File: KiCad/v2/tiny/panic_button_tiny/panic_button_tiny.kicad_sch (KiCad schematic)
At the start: 1 part, among them U1 ESP32-C3

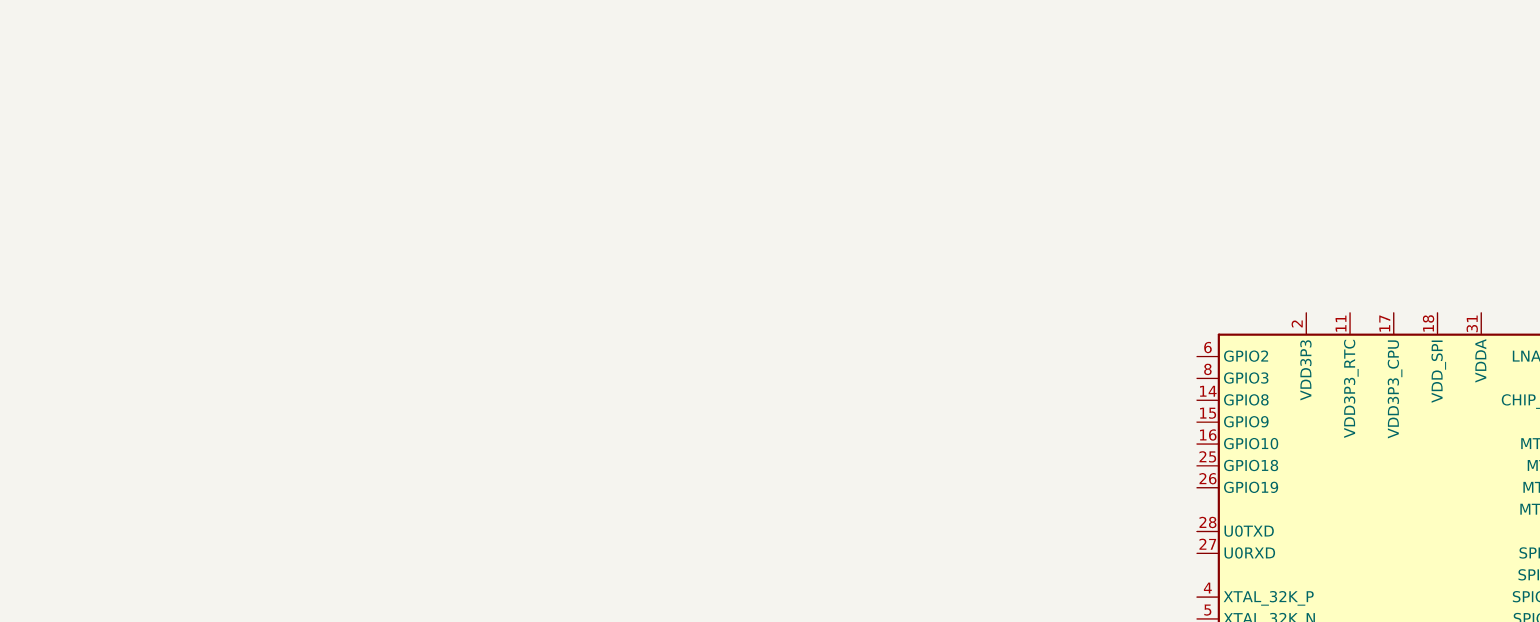
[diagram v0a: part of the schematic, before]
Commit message: [UPDATE] the schematic ot contain some of the components required for creating the device
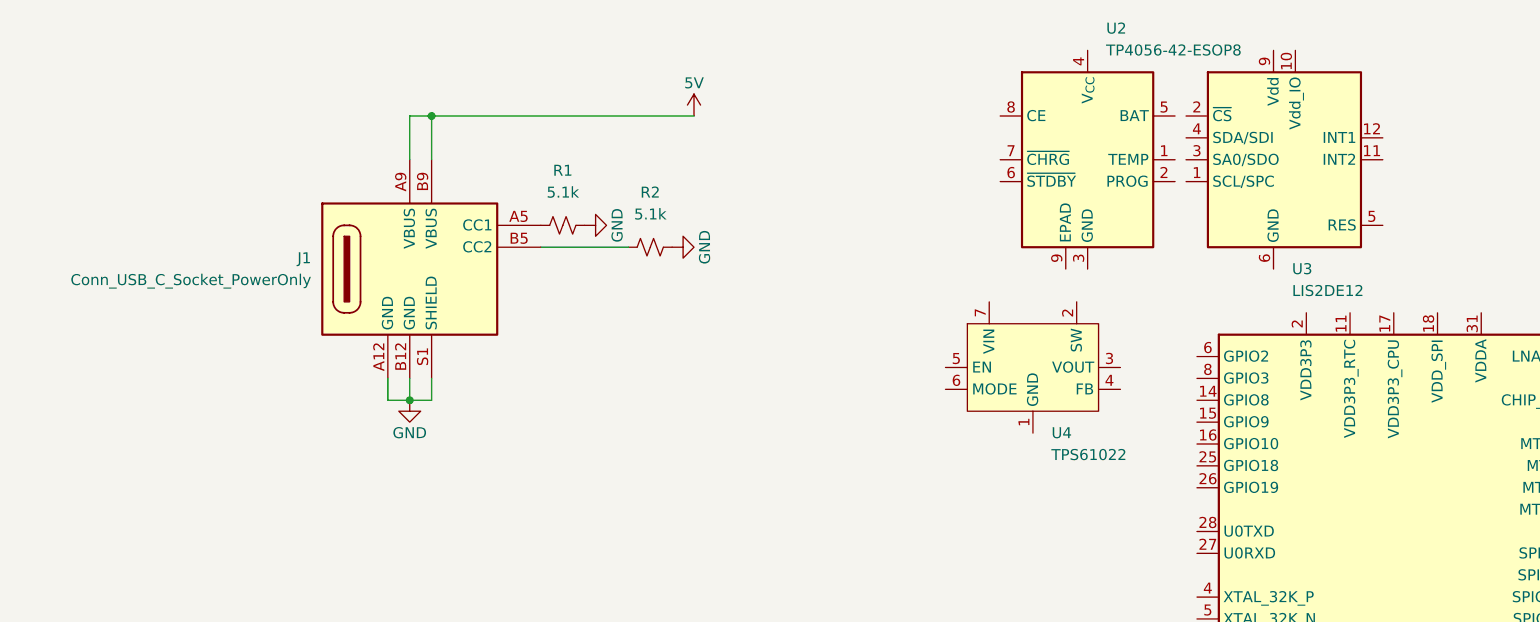
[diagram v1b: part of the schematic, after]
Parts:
- added J1: Conn_USB_C_Socket_PowerOnly, PCM_fab:Conn_USB_C_Socket_GCT_USB4125-GF-A-0190, symbol PCM_fab:Conn_USB_C_Socket_PowerOnly
- added R1, R2: 5.1k, PCM_SparkFun-Resistor:R_0402_1005Metric, symbol PCM_SparkFun-Resistor:5.1k_0402
- added U2: TP4056-42-ESOP8, Package_SO:SOIC-8-1EP_3.9x4.9mm_P1.27mm_EP2.41x3.3mm_ThermalVias, symbol Battery_Management:TP4056-42-ESOP8
- added U3: LIS2DE12, Package_LGA:LGA-12_2x2mm_P0.5mm, symbol Sensor_Motion:LIS2DE12
- added U4: TPS61022, Package_DFN_QFN:Texas_RWU0007A_VQFN-7_2x2mm_P0.5mm, symbol Converter_DCDC:TPS61022
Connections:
- new net: U3.6 (GND), U3.7 (GND), U3.8 (GND)
- new net: J1.A5 (CC1), R1.1
- new net: J1.B5 (CC2), R2.1
- new net 5V: J1.A9 (VBUS), J1.B9 (VBUS)
- new net GND: J1.A12 (GND), J1.B12 (GND), J1.S1 (SHIELD), R1.2, R2.2

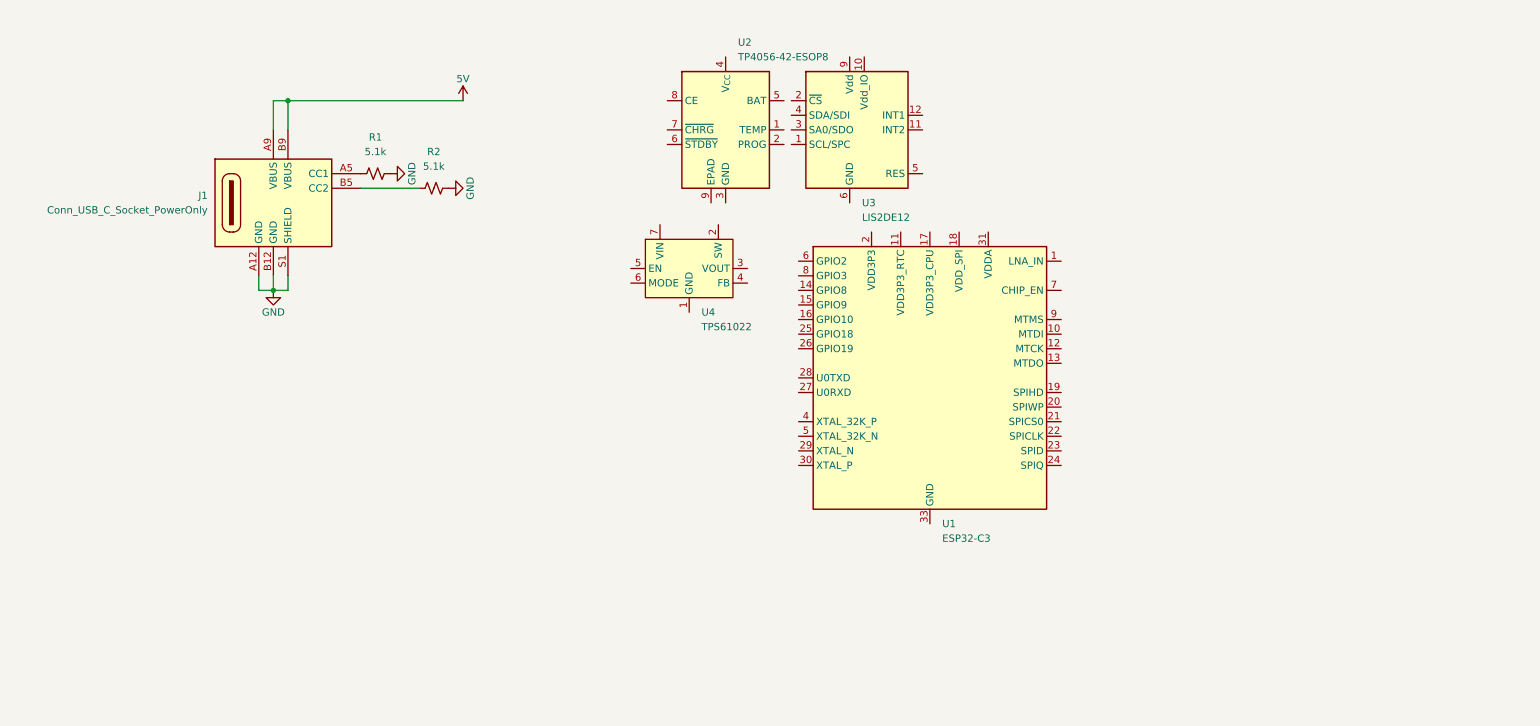
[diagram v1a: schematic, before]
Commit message: [ADD] structure to the components used in the project
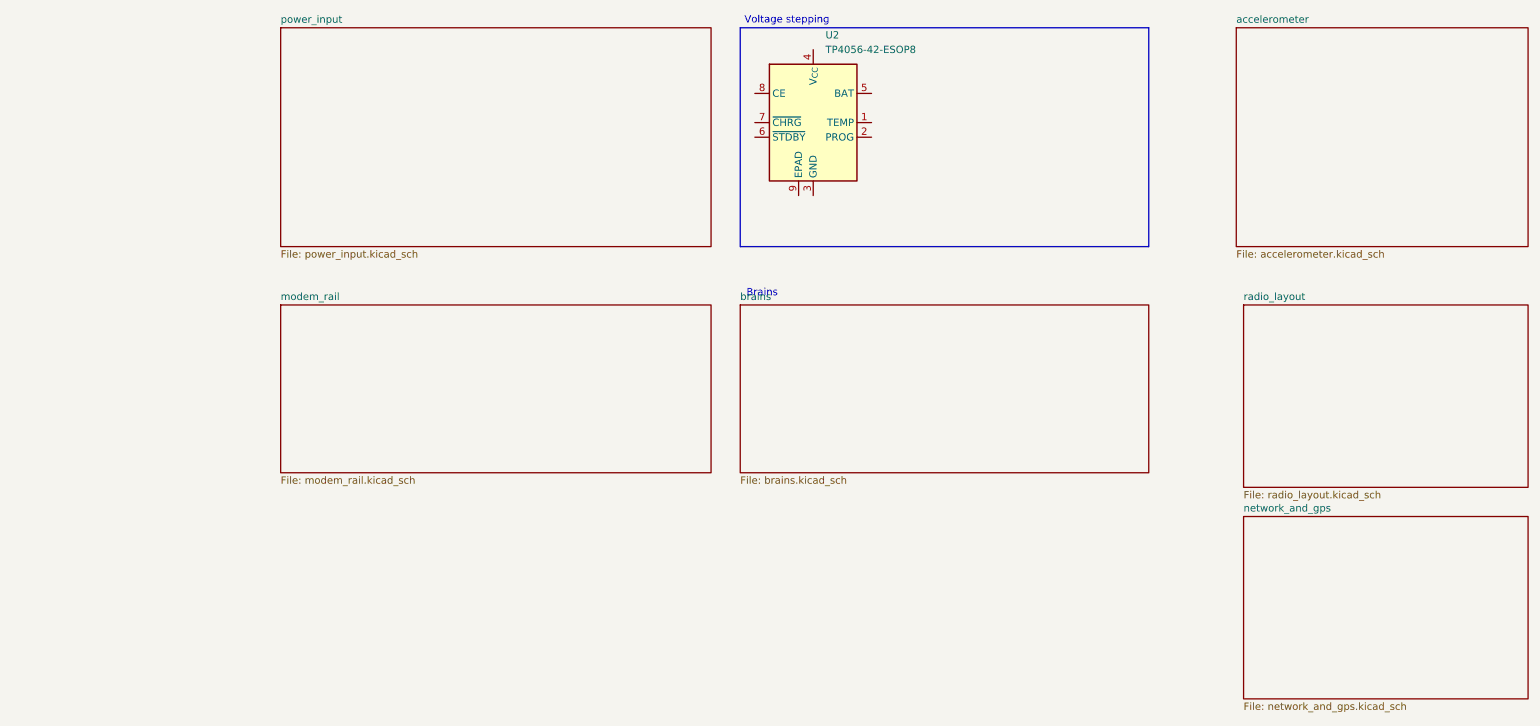
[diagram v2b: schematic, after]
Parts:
- removed J1: Conn_USB_C_Socket_PowerOnly, PCM_fab:Conn_USB_C_Socket_GCT_USB4125-GF-A-0190, symbol PCM_fab:Conn_USB_C_Socket_PowerOnly
- removed R1, R2: 5.1k, PCM_SparkFun-Resistor:R_0402_1005Metric, symbol PCM_SparkFun-Resistor:5.1k_0402
- removed U1: ESP32-C3, Package_DFN_QFN:QFN-32-1EP_5x5mm_P0.5mm_EP3.7x3.7mm, symbol MCU_Espressif:ESP32-C3
- removed U3: LIS2DE12, Package_LGA:LGA-12_2x2mm_P0.5mm, symbol Sensor_Motion:LIS2DE12
- removed U4: TPS61022, Package_DFN_QFN:Texas_RWU0007A_VQFN-7_2x2mm_P0.5mm, symbol Converter_DCDC:TPS61022
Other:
- added sheet accelerometer (accelerometer.kicad_sch)
- added sheet brains (brains.kicad_sch)
- added sheet modem_rail (modem_rail.kicad_sch)
- added sheet network_and_gps (network_and_gps.kicad_sch)
- added sheet power_input (power_input.kicad_sch)
- added sheet radio_layout (radio_layout.kicad_sch)
- note added: "Brains"
- note added: "Voltage stepping"
- moved on the sheet: U2

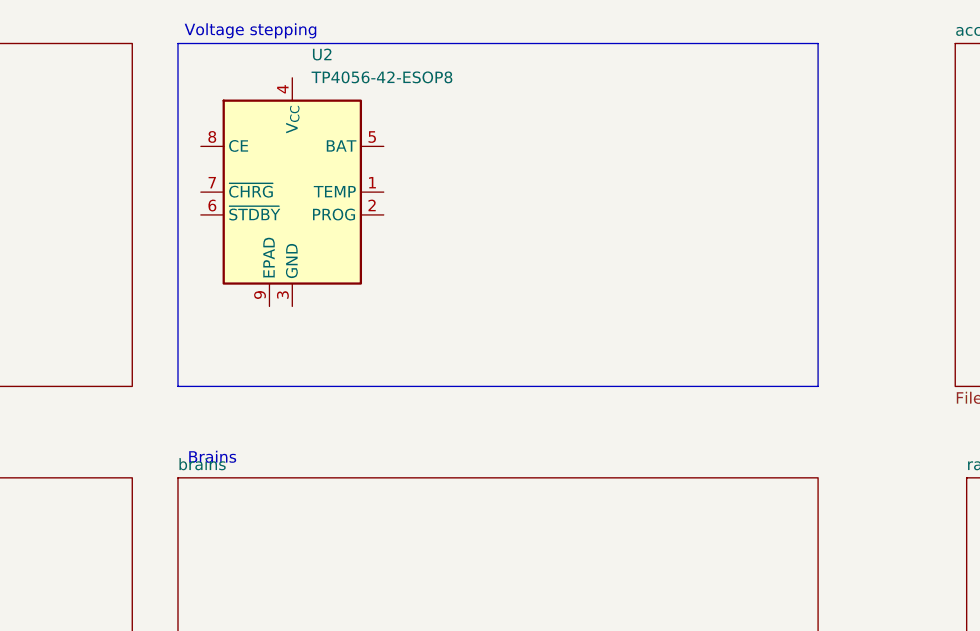
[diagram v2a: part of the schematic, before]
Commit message: [UPDATE] the structure of the KiCad design for the tiny version
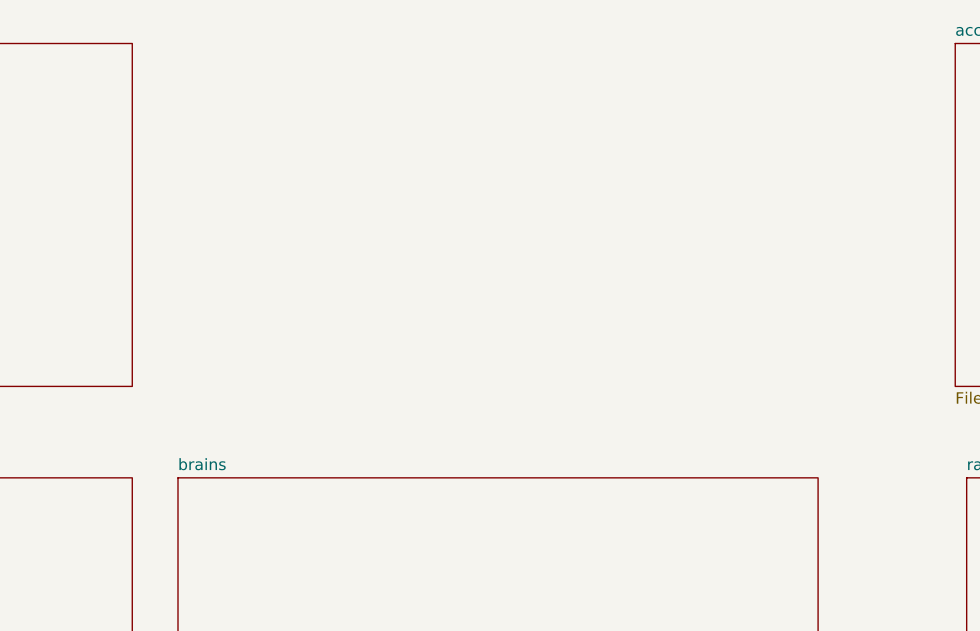
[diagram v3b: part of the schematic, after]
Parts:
- removed U2: TP4056-42-ESOP8, Package_SO:SOIC-8-1EP_3.9x4.9mm_P1.27mm_EP2.41x3.3mm_ThermalVias, symbol Battery_Management:TP4056-42-ESOP8
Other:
- note removed: "Brains"
- note removed: "Voltage stepping"
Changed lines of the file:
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@@
 	(generator_version "10.0")
 	(paper "A4")
-	(rectangle
-		(start 128.27 30.48)
-		(end 199.39 68.58)
-		(stroke
-			(width 0)
-			(type default)
-		)
-		(fill
-			(type none)
-		)
-	)
-	(text "Voltage stepping"
-		(exclude_from_sim no)
-		(at 136.398 29.21 0)
-		(effects
-			(font
-				(size 1.27 1.27)
-			)
-		)
-	)
-	(text "Brains"
-		(exclude_from_sim no)
-		(at 132.08 76.708 0)
-		(effects
-			(font
-				(size 1.27 1.27)
-			)
-		)
-	)
-	(symbol
-		(lib_id "Battery_Management:TP4056-42-ESOP8")
-		(at 140.97 46.99 0)
-		(unit 1)
-		(body_style 1)
-		(exclude_from_sim no)
-		(in_bom yes)
-		(on_board yes)
-		(in_pos_files yes)
-		(dnp no)
-		(fields_autoplaced yes)
-		(property "Reference" "U2"
-			(at 143.1133 31.75 0)
-			(show_name no)
-			(do_not_autoplace no)
-			(effects
-				(font
-					(size 1.27 1.27)
-				)
-				(justify left)
-			)
-		)
-		(property "Value" "TP4056-42-ESOP8"
-			(at 143.1133 34.29 0)
-			(show_name no)
-			(do_not_autoplace no)
-			(effects
-				(font
-					(size 1.27 1.27)
-				)
-				(justify left)
-			)
-		)
-		(property "Footprint" "Package_SO:SOIC-8-1EP_3.9x4.9mm_P1.27mm_EP2.41x3.3mm_ThermalVias"
-			(at 141.478 69.85 0)
-			(hide yes)
-			(show_name no)
-			(do_not_autoplace no)
-			(effects
-				(font
-					(size 1.27 1.27)
-				)
-			)
-		)
-		(property "Datasheet" "https://www.lcsc.com/datasheet/lcsc_datasheet_2410121619_TOPPOWER-Nanjing-Extension-Microelectronics-TP4056-42-ESOP8_C16581.pdf"
-			(at 140.97 72.39 0)
-			(hide yes)
-			(show_name no)
-			(do_not_autoplace no)
-			(effects
-				(font
-					(size 1.27 1.27)
-				)
-			)
-		)
-		(property "Description" "1A Standalone Linear Li-ion/LiPo single-cell battery charger, 4.2V ±1% charge voltage, VCC = 4.0..8.0V, SOIC-8 (SOP-8)"
-			(at 141.478 67.31 0)
-			(hide yes)
-			(show_name no)
-			(do_not_autoplace no)
-			(effects
-				(font
-					(size 1.27 1.27)
-				)
-			)
-		)
-		(pin "9"
-		)
-		(pin "4"
-		)
-		(pin "3"
-		)
-		(pin "2"
-		)
-		(pin "1"
-		)
-		(pin "7"
-		)
-		(pin "6"
-		)
-		(pin "5"
-		)
-		(pin "8"
-		)
-		(instances
-			(project "panic_button_tiny"
-				(path "/c4eb92e9-b42f-4db0-b1d9-0ef70f7ca601"
-					(reference "U2")
-					(unit 1)
-				)
-			)
-		)
-	)
 	(sheet
 		(at 215.9 115.57)

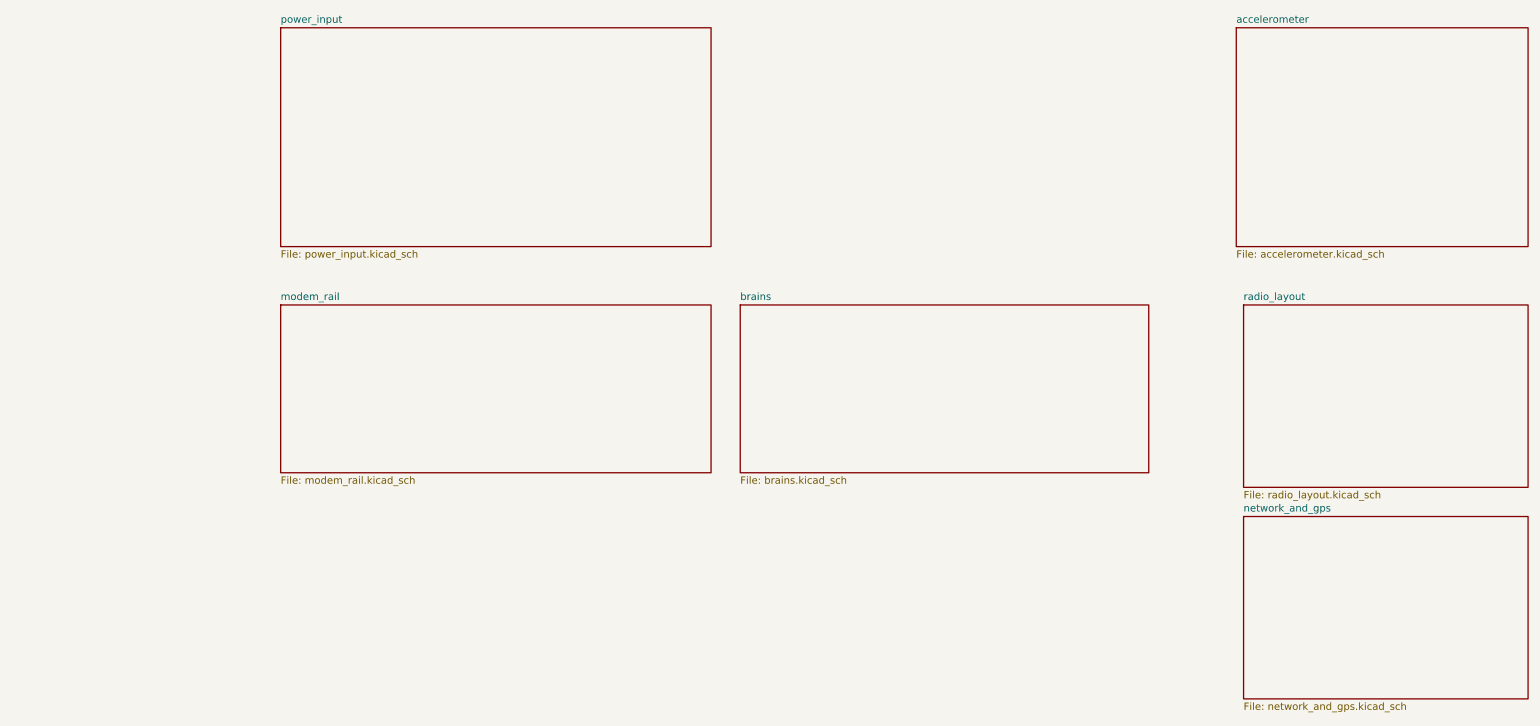
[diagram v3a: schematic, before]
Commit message: [UPDATE] the schematic with a buzzer and wirering for the different components
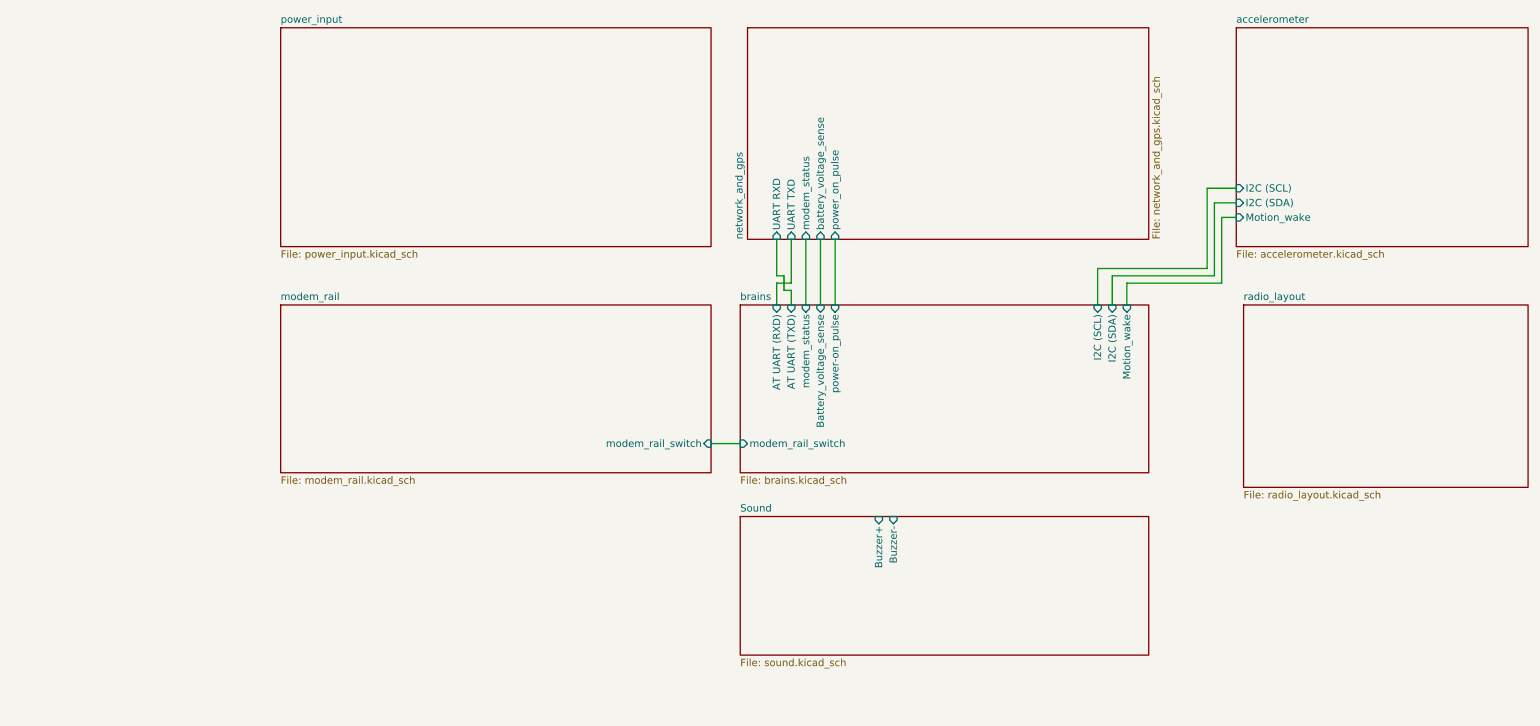
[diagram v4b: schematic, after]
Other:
- added sheet Sound (sound.kicad_sch)
- sheet accelerometer ports: added I2C (SCL), I2C (SDA), Motion_wake; removed none
- sheet brains ports: added AT UART (RXD), AT UART (TXD), Battery_voltage_sense, I2C (SCL), I2C (SDA), Motion_wake, modem_rail_switch, modem_status, power-on_pulse; removed none
- sheet modem_rail ports: added modem_rail_switch; removed none
- sheet network_and_gps ports: added UART RXD, UART TXD, battery_voltage_sense, modem_status, power_on_pulse; removed none

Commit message: [UPDATE] the schematic to contain more connections for the battery section
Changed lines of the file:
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@@
 		)
 		(property "Sheetname" "Sound"
-			(at 128.27 114.8584 0)
+			(at 127.5584 139.7 90)
 			(show_name no)
 			(do_not_autoplace no)
@@
 		)
 		(property "Sheetfile" "sound.kicad_sch"
-			(at 128.27 140.2846 0)
+			(at 199.9746 139.7 90)
 			(show_name no)
 			(do_not_autoplace no)
